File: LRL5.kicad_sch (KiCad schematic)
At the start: 30 parts, among them J1 POWER, J2 On/Off, J5 OUT, J6 MODE, Q1 BC549, U1 BA033CC0T, U2 NHD-C0220BIZ

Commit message: Change some texts
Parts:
- Q1: footprint Package_TO_SOT_THT:TO-92_HandSolder -> Package_TO_SOT_THT:TO-126-3_Vertical
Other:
- note added: "B8"
- note added: "B9"
- note removed: "PB8"
- note removed: "PB9"
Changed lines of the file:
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@@
 		)
 	)
-	(text "PB9"
-		(exclude_from_sim no)
-		(at 246.38 41.91 0)
+	(text "B9"
+		(exclude_from_sim no)
+		(at 247.015 41.91 0)
 		(effects
 			(font
@@
 		)
 	)
-	(text "PB8"
-		(exclude_from_sim no)
-		(at 246.38 44.45 0)
+	(text "B8"
+		(exclude_from_sim no)
+		(at 247.015 44.45 0)
 		(effects
 			(font
@@
 			)
 		)
-		(property "Footprint" "Package_TO_SOT_THT:TO-92_HandSolder"
+		(property "Footprint" "Package_TO_SOT_THT:TO-126-3_Vertical"
 			(at 62.23 155.575 0)
 			(effects

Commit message: Added filled zone
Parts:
- J3, J4: footprint Connector_PinHeader_2.54mm:PinHeader_1x20_P2.54mm_Vertical -> Connector_PinHeader_2.54mm:PinHeader_1x20_P2.54mm_Vertical_SMD_Pin1Left
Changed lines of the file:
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@@
 			)
 		)
-		(property "Footprint" "Connector_PinHeader_2.54mm:PinHeader_1x20_P2.54mm_Vertical"
+		(property "Footprint" "Connector_PinHeader_2.54mm:PinHeader_1x20_P2.54mm_Vertical_SMD_Pin1Left"
 			(at 250.19 57.15 0)
 			(effects
@@
 			)
 		)
-		(property "Footprint" "Connector_PinHeader_2.54mm:PinHeader_1x20_P2.54mm_Vertical"
+		(property "Footprint" "Connector_PinHeader_2.54mm:PinHeader_1x20_P2.54mm_Vertical_SMD_Pin1Left"
 			(at 231.14 57.15 0)
 			(effects

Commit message: Some fixes
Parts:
- H1, H2, H3, H4: footprint MountingHole:MountingHole_2.5mm -> MountingHole:MountingHole_3.2mm_M3
- J2: footprint Connector_PinHeader_2.54mm:PinHeader_1x02_P2.54mm_Vertical -> Connector_PinHeader_2.54mm:PinHeader_1x02_P2.54mm_Vertical_SMD_Pin1Left
- J5: footprint Connector_PinHeader_2.54mm:PinHeader_1x03_P2.54mm_Vertical -> Connector_PinHeader_2.54mm:PinHeader_1x03_P2.54mm_Vertical_SMD_Pin1Left
- J6: footprint Connector_PinHeader_2.54mm:PinHeader_1x04_P2.54mm_Vertical -> Connector_PinHeader_2.54mm:PinHeader_1x04_P2.54mm_Vertical_SMD_Pin1Left
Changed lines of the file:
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@@
 			)
 		)
-		(property "Footprint" "MountingHole:MountingHole_2.5mm"
+		(property "Footprint" "MountingHole:MountingHole_3.2mm_M3"
 			(at 25.4 104.14 0)
 			(effects
@@
 			)
 		)
-		(property "Footprint" "Connector_PinHeader_2.54mm:PinHeader_1x02_P2.54mm_Vertical"
+		(property "Footprint" "Connector_PinHeader_2.54mm:PinHeader_1x02_P2.54mm_Vertical_SMD_Pin1Left"
 			(at 247.65 121.92 0)
 			(effects
@@
 			)
 		)
-		(property "Footprint" "MountingHole:MountingHole_2.5mm"
+		(property "Footprint" "MountingHole:MountingHole_3.2mm_M3"
 			(at 25.4 109.22 0)
 			(effects
@@
 			)
 		)
-		(property "Footprint" "MountingHole:MountingHole_2.5mm"
+		(property "Footprint" "MountingHole:MountingHole_3.2mm_M3"
 			(at 25.4 99.06 0)
 			(effects
@@
 			)
 		)
-		(property "Footprint" "MountingHole:MountingHole_2.5mm"
+		(property "Footprint" "MountingHole:MountingHole_3.2mm_M3"
 			(at 25.4 93.98 0)
 			(effects
@@
 			)
 		)
-		(property "Footprint" "Connector_PinHeader_2.54mm:PinHeader_1x04_P2.54mm_Vertical"
+		(property "Footprint" "Connector_PinHeader_2.54mm:PinHeader_1x04_P2.54mm_Vertical_SMD_Pin1Left"
 			(at 189.23 40.64 0)
 			(effects
@@
 			)
 		)
-		(property "Footprint" "Connector_PinHeader_2.54mm:PinHeader_1x03_P2.54mm_Vertical"
+		(property "Footprint" "Connector_PinHeader_2.54mm:PinHeader_1x03_P2.54mm_Vertical_SMD_Pin1Left"
 			(at 91.44 147.32 0)
 			(effects

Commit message: Some fixes 2
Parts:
- added J7: DEBUG, Connector_PinHeader_2.54mm:PinHeader_1x03_P2.54mm_Vertical_SMD_Pin1Left, symbol Connector_Generic:Conn_01x03
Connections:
- net GND: now also J7.3 (Pin_3)
- net UART1_RX: now reaches J3.14 (Pin_14)
- net UART1_RX: now also J7.2 (Pin_2)
- net UART1_TX: now reaches J3.15 (Pin_15)
- net UART1_TX: now also J7.1 (Pin_1)
- no-connect marks 29 -> 27
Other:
- moved on the sheet: R8

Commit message: Add DEBUG connector
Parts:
- J6: footprint Connector_PinHeader_2.54mm:PinHeader_1x04_P2.54mm_Vertical_SMD_Pin1Left -> Connector_PinHeader_2.54mm:PinHeader_1x04_P2.54mm_Vertical
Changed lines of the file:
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@@
 			)
 		)
-		(property "Footprint" "Connector_PinHeader_2.54mm:PinHeader_1x04_P2.54mm_Vertical_SMD_Pin1Left"
+		(property "Footprint" "Connector_PinHeader_2.54mm:PinHeader_1x04_P2.54mm_Vertical"
 			(at 189.23 40.64 0)
 			(effects

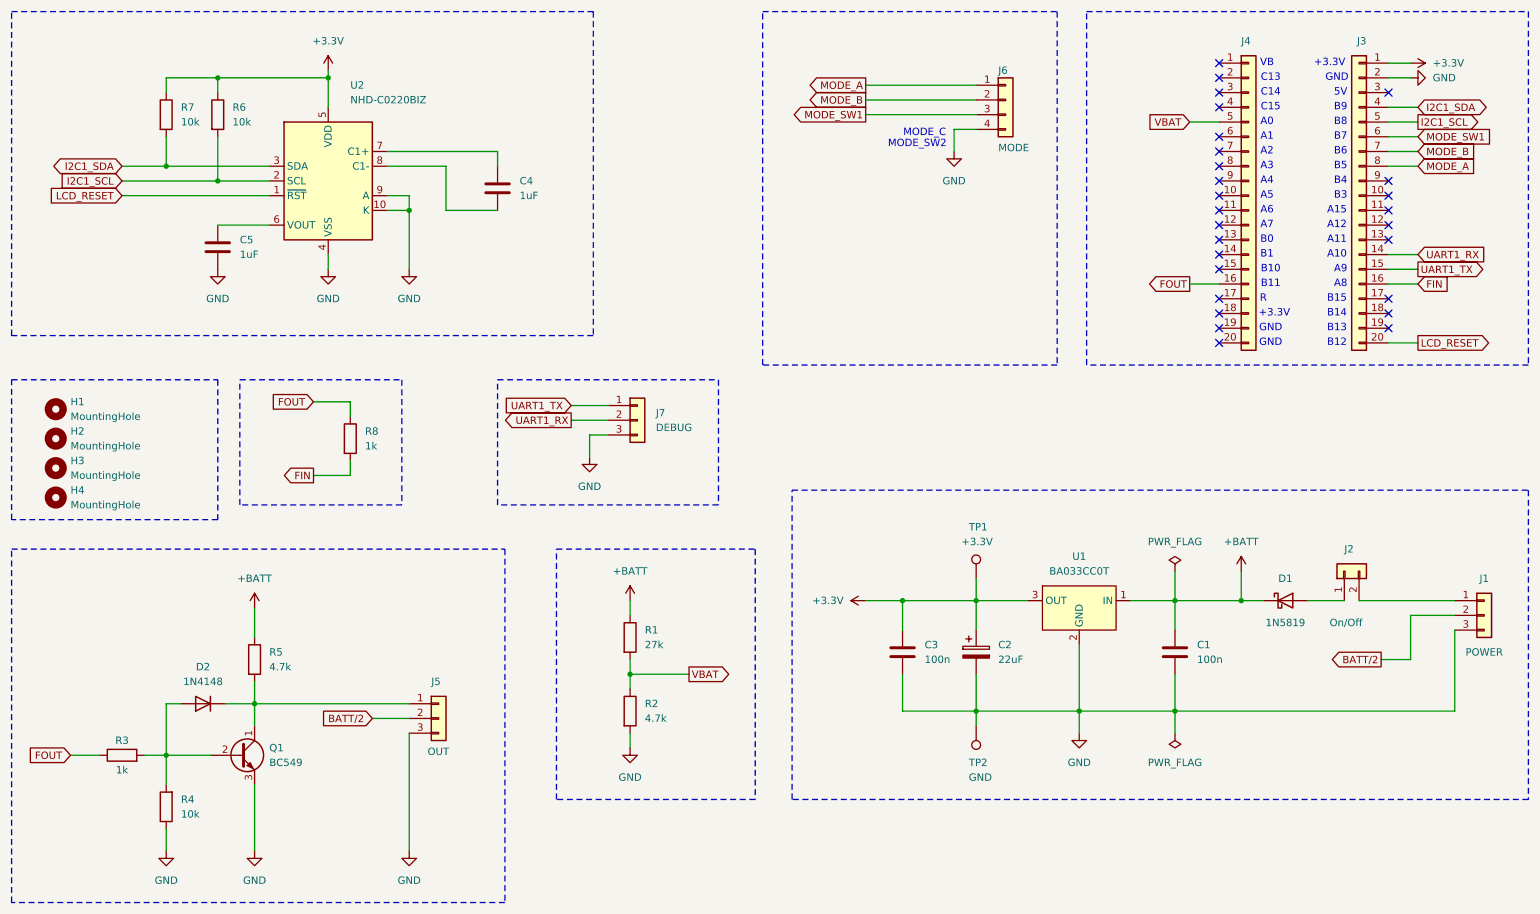
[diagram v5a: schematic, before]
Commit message: Add User Button
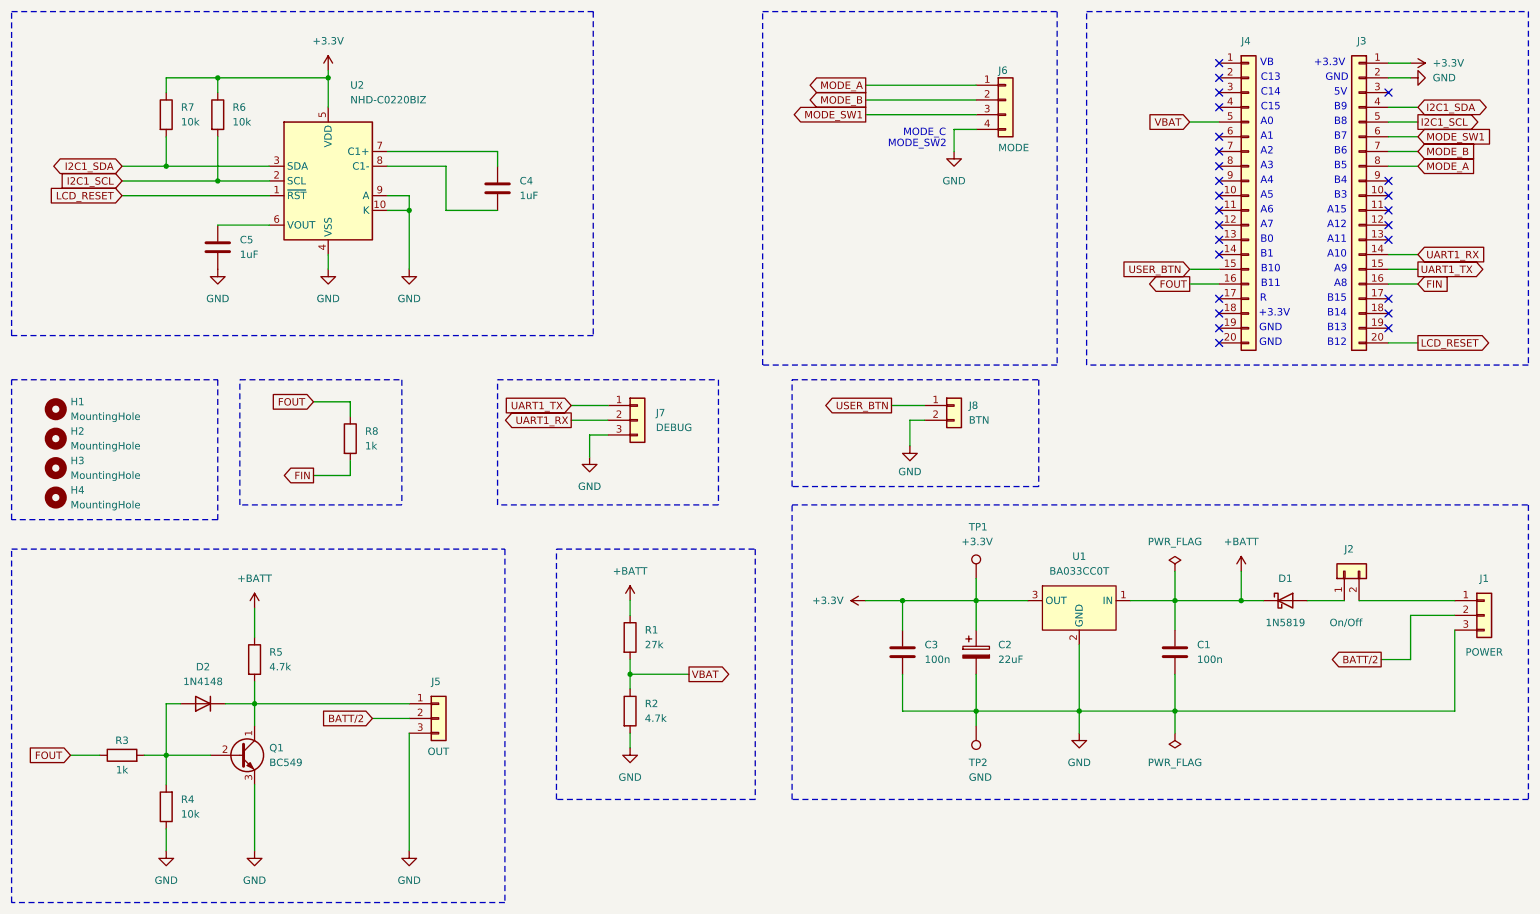
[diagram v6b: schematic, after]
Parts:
- added J8: BTN, Connector_PinHeader_2.54mm:PinHeader_1x02_P2.54mm_Vertical_SMD_Pin1Left, symbol Connector_Generic:Conn_01x02
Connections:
- net GND: now also J8.2 (Pin_2)
- net USER_BTN: now reaches J4.15 (Pin_15)
- net USER_BTN: now also J8.1 (Pin_1)
- no-connect marks 27 -> 26
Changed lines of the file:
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@@
 	)
 	(no_connect
-		(at 226.06 69.85)
-	)
-	(no_connect
 		(at 255.27 59.69)
 	)
@@
 	(wire
 		(pts
+			(xy 175.26 95.885) (xy 172.72 95.885)
+		)
+		(stroke
+			(width 0)
+			(type default)
+		)
+	)
+	(wire
+		(pts
 			(xy 255.27 34.29) (xy 259.08 34.29)
 		)
@@
 	(wire
 		(pts
+			(xy 220.98 69.85) (xy 226.06 69.85)
+		)
+		(stroke
+			(width 0)
+			(type default)
+		)
+	)
+	(wire
+		(pts
 			(xy 250.19 127) (xy 266.7 127)
 		)
@@
 	(wire
 		(pts
+			(xy 169.545 93.345) (xy 175.26 93.345)
+		)
+		(stroke
+			(width 0)
+			(type default)
+		)
+	)
+	(wire
+		(pts
 			(xy 201.93 146.05) (xy 201.93 149.86)
 		)
@@
 	(wire
 		(pts
+			(xy 172.72 95.885) (xy 172.72 100.33)
+		)
+		(stroke
+			(width 0)
+			(type default)
+		)
+	)
+	(wire
+		(pts
 			(xy 255.27 41.91) (xy 260.35 41.91)
 		)
@@
 	)
 	(rectangle
-		(start 152.4 107.95)
+		(start 152.4 110.49)
 		(end 279.4 161.29)
 		(stroke
@@
 	)
 	(rectangle
+		(start 152.4 88.9)
+		(end 194.945 107.315)
+		(stroke
+			(width 0)
+			(type dash)
+		)
+		(fill
+			(type none)
+		)
+	)
+	(rectangle
 		(start 203.2 25.4)
 		(end 279.4 86.36)
@@
 		)
 	)
+	(global_label "USER_BTN"
+		(shape input)
+		(at 220.98 69.85 180)
+		(fields_autoplaced yes)
+		(effects
+			(font
+				(size 1.27 1.27)
+			)
+			(justify right)
+		)
+		(property "Intersheetrefs" "${INTERSHEET_REFS}"
+			(at 208.5001 69.85 0)
+			(effects
+				(font
+					(size 1.27 1.27)
+				)
+				(justify right)
+				(hide yes)
+			)
+		)
+	)
 	(global_label "MODE_B"
 		(shape input)
@@
 		)
 	)
+	(global_label "USER_BTN"
+		(shape output)
+		(at 169.545 93.345 180)
+		(fields_autoplaced yes)
+		(effects
+			(font
+				(size 1.27 1.27)
+			)
+			(justify right)
+		)
+		(property "Intersheetrefs" "${INTERSHEET_REFS}"
+			(at 157.0651 93.345 0)
+			(effects
+				(font
+					(size 1.27 1.27)
+				)
+				(justify right)
+				(hide yes)
+			)
+		)
+	)
 	(global_label "UART1_RX"
 		(shape output)
@@
 	)
 	(symbol
+		(lib_id "Connector_Generic:Conn_01x02")
+		(at 180.34 93.345 0)
+		(unit 1)
+		(exclude_from_sim no)
+		(in_bom yes)
+		(on_board yes)
+		(dnp no)
+		(fields_autoplaced yes)
+		(property "Reference" "J8"
+			(at 182.88 93.3449 0)
+			(effects
+				(font
+					(size 1.27 1.27)
+				)
+				(justify left)
+			)
+		)
+		(property "Value" "BTN"
+			(at 182.88 95.8849 0)
+			(effects
+				(font
+					(size 1.27 1.27)
+				)
+				(justify left)
+			)
+		)
+		(property "Footprint" "Connector_PinHeader_2.54mm:PinHeader_1x02_P2.54mm_Vertical_SMD_Pin1Left"
+			(at 180.34 93.345 0)
+			(effects
+				(font
+					(size 1.27 1.27)
+				)
+				(hide yes)
+			)
+		)
+		(property "Datasheet" "~"
+			(at 180.34 93.345 0)
+			(effects
+				(font
+					(size 1.27 1.27)
+				)
+				(hide yes)
+			)
+		)
+		(property "Description" "Generic connector, single row, 01x02, script generated (kicad-library-utils/schlib/autogen/connector/)"
+			(at 180.34 93.345 0)
+			(effects
+				(font
+					(size 1.27 1.27)
+				)
+				(hide yes)
+			)
+		)
+		(pin "2"
+		)
+		(pin "1"
+		)
+		(instances
+			(project ""
+				(path "/ffc94b8d-ae8a-4b9a-afc3-af60dc91e04f"
+					(reference "J8")
+					(unit 1)
+				)
+			)
+		)
+	)
+	(symbol
 		(lib_id "power:+BATT")
 		(at 59.69 128.27 0)
@@
 					(unit 1)
 				)
+			)
+		)
+	)
+	(symbol
+		(lib_id "power:GND")
+		(at 172.72 100.33 0)
+		(unit 1)
+		(exclude_from_sim no)
+		(in_bom yes)
+		(on_board yes)
+		(dnp no)
+		(fields_autoplaced yes)
+		(property "Reference" "#PWR014"
+			(at 172.72 106.68 0)
+			(effects
+				(font
+					(size 1.27 1.27)
+				)
+				(hide yes)
+			)
+		)
+		(property "Value" "GND"
+			(at 172.72 104.775 0)
+			(effects
+				(font
+					(size 1.27 1.27)
+				)
+			)
+		)
+		(property "Footprint" ""
+			(at 172.72 100.33 0)
+			(effects
+				(font
+					(size 1.27 1.27)
+				)
+				(hide yes)
+			)
+		)
+		(property "Datasheet" ""
+			(at 172.72 100.33 0)
+			(effects
+				(font
+					(size 1.27 1.27)
+				)
+				(hide yes)
+			)
+		)
+		(property "Description" "Power symbol creates a global label with name \"GND\" , ground"
+			(at 172.72 100.33 0)
+			(effects
+				(font
+					(size 1.27 1.27)
+				)
+				(hide yes)
+			)
+		)
+		(pin "1"
+		)
+		(instances
+			(project ""
+				(path "/ffc94b8d-ae8a-4b9a-afc3-af60dc91e04f"
+					(reference "#PWR014")
+					(unit 1)
+				)

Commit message: Add profuction files
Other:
- moved on the sheet: J7, J8
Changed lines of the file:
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@@
 	(wire
 		(pts
+			(xy 168.91 93.98) (xy 175.26 93.98)
+		)
+		(stroke
+			(width 0)
+			(type default)
+		)
+	)
+	(wire
+		(pts
 			(xy 44.45 144.78) (xy 46.99 144.78)
 		)
@@
 	(wire
 		(pts
+			(xy 115.57 93.98) (xy 124.46 93.98)
+		)
+		(stroke
+			(width 0)
+			(type default)
+		)
+	)
+	(wire
+		(pts
 			(xy 184.15 139.7) (xy 184.15 146.05)
 		)
@@
 	(wire
 		(pts
+			(xy 172.72 100.33) (xy 172.72 96.52)
+		)
+		(stroke
+			(width 0)
+			(type default)
+		)
+	)
+	(wire
+		(pts
 			(xy 44.45 144.78) (xy 44.45 153.67)
 		)
@@
 	(wire
 		(pts
+			(xy 124.46 99.06) (xy 118.11 99.06)
+		)
+		(stroke
+			(width 0)
+			(type default)
+		)
+	)
+	(wire
+		(pts
+			(xy 172.72 96.52) (xy 175.26 96.52)
+		)
+		(stroke
+			(width 0)
+			(type default)
+		)
+	)
+	(wire
+		(pts
 			(xy 72.39 36.83) (xy 53.34 36.83)
 		)
@@
 	(wire
 		(pts
+			(xy 115.57 96.52) (xy 124.46 96.52)
+		)
+		(stroke
+			(width 0)
+			(type default)
+		)
+	)
+	(wire
+		(pts
 			(xy 165.1 127) (xy 171.45 127)
 		)
@@
 	(wire
 		(pts
-			(xy 114.3 95.885) (xy 120.65 95.885)
-		)
-		(stroke
-			(width 0)
-			(type default)
-		)
-	)
-	(wire
-		(pts
 			(xy 229.87 127) (xy 233.68 127)
 		)
@@
 	(wire
 		(pts
-			(xy 114.3 93.345) (xy 120.65 93.345)
-		)
-		(stroke
-			(width 0)
-			(type default)
-		)
-	)
-	(wire
-		(pts
 			(xy 86.36 57.15) (xy 86.36 59.69)
 		)
@@
 	(wire
 		(pts
-			(xy 117.475 98.425) (xy 120.65 98.425)
-		)
-		(stroke
-			(width 0)
-			(type default)
-		)
-	)
-	(wire
-		(pts
 			(xy 36.83 54.61) (xy 53.34 54.61)
 		)
@@
 	(wire
 		(pts
-			(xy 175.26 95.885) (xy 172.72 95.885)
-		)
-		(stroke
-			(width 0)
-			(type default)
-		)
-	)
-	(wire
-		(pts
 			(xy 255.27 34.29) (xy 259.08 34.29)
 		)
@@
 	(wire
 		(pts
-			(xy 117.475 102.235) (xy 117.475 98.425)
-		)
-		(stroke
-			(width 0)
-			(type default)
-		)
-	)
-	(wire
-		(pts
 			(xy 255.27 69.85) (xy 260.35 69.85)
 		)
@@
 	(wire
 		(pts
-			(xy 169.545 93.345) (xy 175.26 93.345)
+			(xy 201.93 146.05) (xy 201.93 149.86)
 		)
 		(stroke
@@
 	(wire
 		(pts
-			(xy 201.93 146.05) (xy 201.93 149.86)
+			(xy 118.11 99.06) (xy 118.11 101.6)
 		)
 		(stroke
@@
 	(wire
 		(pts
-			(xy 172.72 95.885) (xy 172.72 100.33)
-		)
-		(stroke
-			(width 0)
-			(type default)
-		)
-	)
-	(wire
-		(pts
 			(xy 255.27 41.91) (xy 260.35 41.91)
 		)
@@
 	(rectangle
 		(start 101.6 88.9)
-		(end 139.7 110.49)
+		(end 140.97 110.49)
 		(stroke
 			(width 0)
@@
 	(global_label "USER_BTN"
 		(shape output)
-		(at 169.545 93.345 180)
+		(at 168.91 93.98 180)
 		(fields_autoplaced yes)
 		(effects
@@
 		)
 		(property "Intersheetrefs" "${INTERSHEET_REFS}"
-			(at 157.0651 93.345 0)
+			(at 156.4301 93.98 0)
 			(effects
 				(font
@@
 	(global_label "UART1_RX"
 		(shape output)
-		(at 114.3 95.885 180)
+		(at 115.57 96.52 180)
 		(fields_autoplaced yes)
 		(effects
@@
 		)
 		(property "Intersheetrefs" "${INTERSHEET_REFS}"
-			(at 102.0015 95.885 0)
+			(at 103.2715 96.52 0)
 			(effects
 				(font
@@
 	(global_label "UART1_TX"
 		(shape input)
-		(at 114.3 93.345 180)
+		(at 115.57 93.98 180)
 		(fields_autoplaced yes)
 		(effects
@@
 		)
 		(property "Intersheetrefs" "${INTERSHEET_REFS}"
-			(at 102.3039 93.345 0)
+			(at 103.5739 93.98 0)
 			(effects
 				(font
@@
 	(symbol
 		(lib_id "power:GND")
-		(at 117.475 102.235 0)
+		(at 118.11 101.6 0)
 		(unit 1)
 		(exclude_from_sim no)
@@
 		(fields_autoplaced yes)
 		(property "Reference" "#PWR013"
-			(at 117.475 108.585 0)
+			(at 118.11 107.95 0)
 			(effects
 				(font
@@
 		)
 		(property "Value" "GND"
-			(at 117.475 107.315 0)
+			(at 118.11 106.68 0)
 			(effects
 				(font
@@
 		)
 		(property "Footprint" ""
-			(at 117.475 102.235 0)
+			(at 118.11 101.6 0)
 			(effects
 				(font
@@
 		)
 		(property "Datasheet" ""
-			(at 117.475 102.235 0)
+			(at 118.11 101.6 0)
 			(effects
 				(font
@@
 		)
 		(property "Description" "Power symbol creates a global label with name \"GND\" , ground"
-			(at 117.475 102.235 0)
+			(at 118.11 101.6 0)
 			(effects
 				(font
@@
 	(symbol
 		(lib_id "Connector_Generic:Conn_01x02")
-		(at 180.34 93.345 0)
+		(at 180.34 93.98 0)
 		(unit 1)
 		(exclude_from_sim no)
@@
 		(fields_autoplaced yes)
 		(property "Reference" "J8"
-			(at 182.88 93.3449 0)
+			(at 182.88 93.9799 0)
 			(effects
 				(font
@@
 		)
 		(property "Value" "BTN"
-			(at 182.88 95.8849 0)
+			(at 182.88 96.5199 0)
 			(effects
 				(font
@@
 		)
 		(property "Footprint" "Connector_PinHeader_2.54mm:PinHeader_1x02_P2.54mm_Vertical_SMD_Pin1Left"
-			(at 180.34 93.345 0)
+			(at 180.34 93.98 0)
 			(effects
 				(font
@@
 		)
 		(property "Datasheet" "~"
-			(at 180.34 93.345 0)
+			(at 180.34 93.98 0)
 			(effects
 				(font
@@
 		)
 		(property "Description" "Generic connector, single row, 01x02, script generated (kicad-library-utils/schlib/autogen/connector/)"
-			(at 180.34 93.345 0)
+			(at 180.34 93.98 0)
 			(effects
 				(font
@@
 	(symbol
 		(lib_id "Connector_Generic:Conn_01x03")
-		(at 125.73 95.885 0)
+		(at 129.54 96.52 0)
 		(unit 1)
 		(exclude_from_sim no)
@@
 		(fields_autoplaced yes)
 		(property "Reference" "J7"
-			(at 128.905 94.6149 0)
+			(at 132.715 95.2499 0)
 			(effects
 				(font
@@
 		)
 		(property "Value" "DEBUG"
-			(at 128.905 97.1549 0)
+			(at 132.715 97.7899 0)
 			(effects
 				(font
@@
 		)
 		(property "Footprint" "Connector_PinHeader_2.54mm:PinHeader_1x03_P2.54mm_Vertical_SMD_Pin1Left"
-			(at 125.73 95.885 0)
+			(at 129.54 96.52 0)
 			(effects
 				(font
@@
 		)
 		(property "Datasheet" "~"
-			(at 125.73 95.885 0)
+			(at 129.54 96.52 0)
 			(effects
 				(font
@@
 		)
 		(property "Description" "Generic connector, single row, 01x03, script generated (kicad-library-utils/schlib/autogen/connector/)"
-			(at 125.73 95.885 0)
+			(at 129.54 96.52 0)
 			(effects
 				(font
